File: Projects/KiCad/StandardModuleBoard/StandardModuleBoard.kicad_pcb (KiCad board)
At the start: 2 copper layers, 110 x 95 mm, 20 parts, among them J1 Conn_01x04_Pin, J2 Conn_01x04_Socket, J3 Micro_SD_Card_Det_Hirose_DM3AT, U1 NUCLEO-F303K8, U2 MCP2562-E-P, U3 24LC256

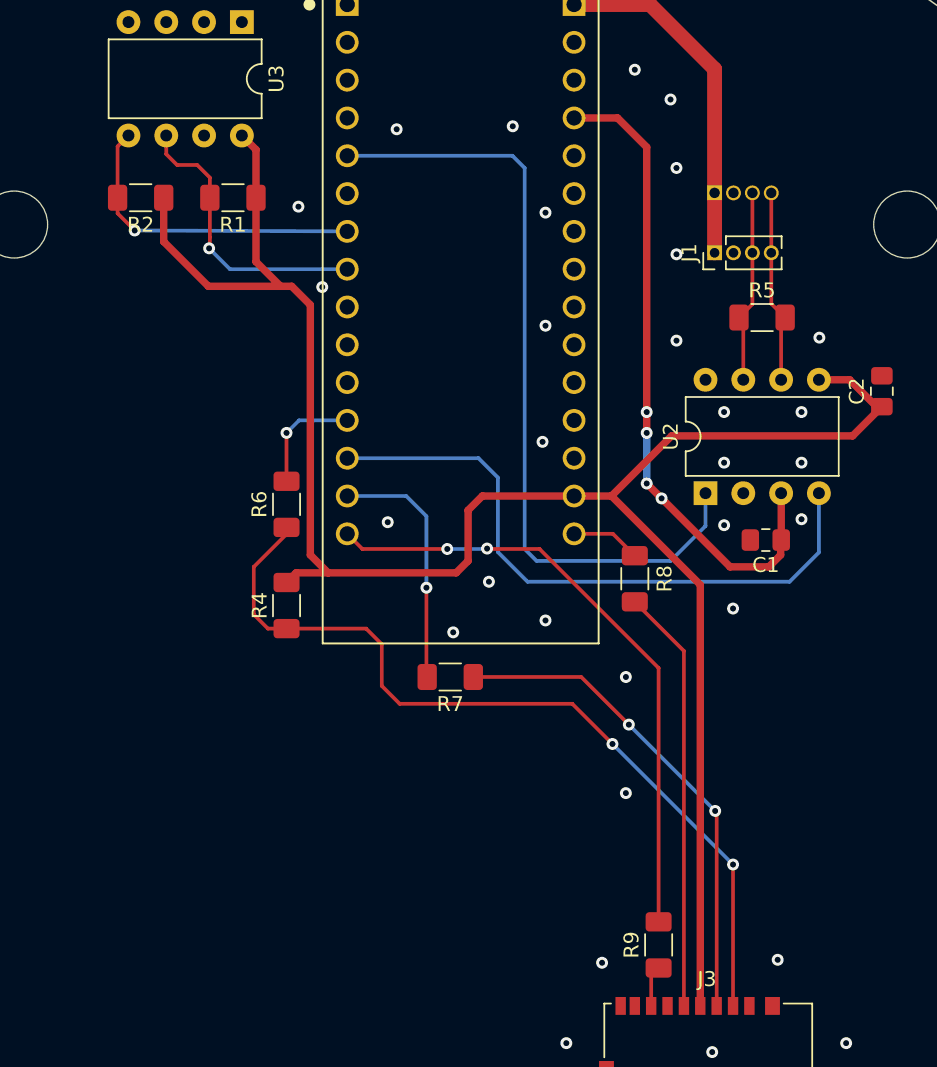
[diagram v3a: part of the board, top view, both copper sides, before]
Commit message: 標準モジュールにパイロットランプを追加
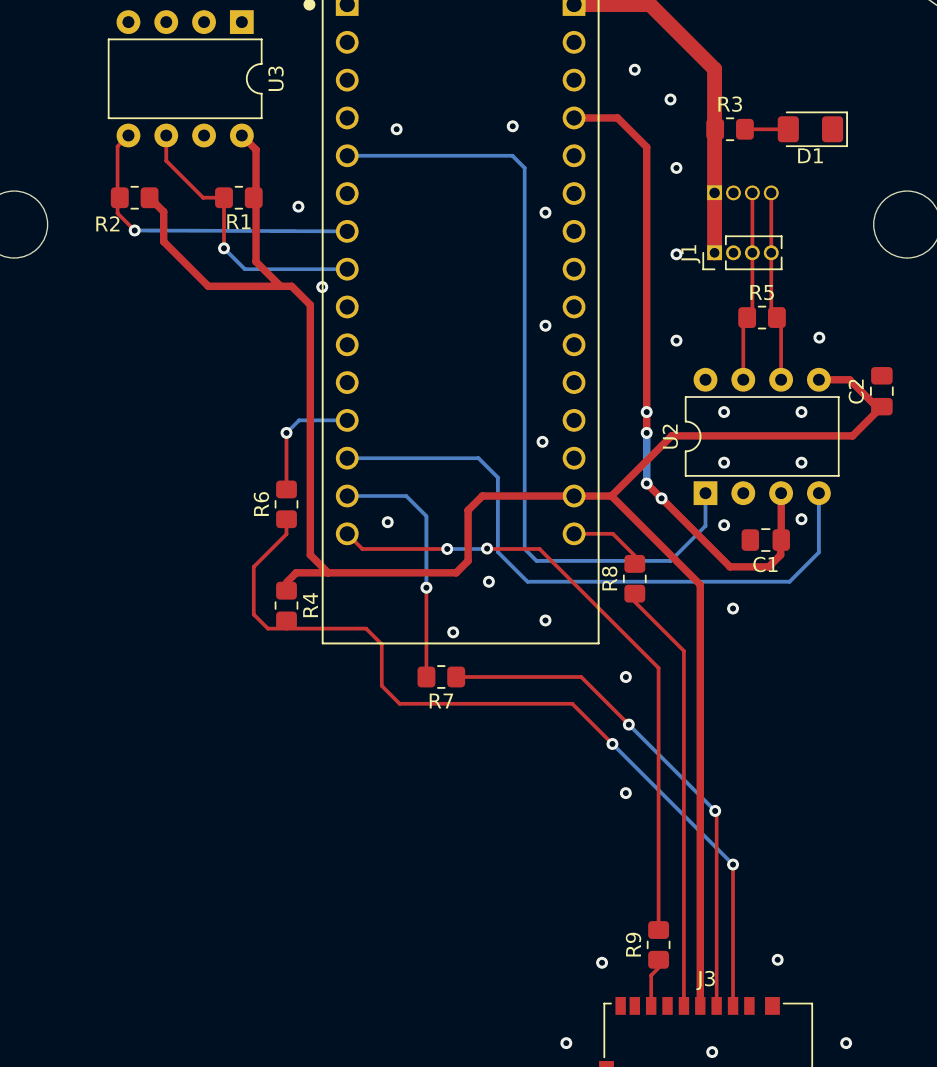
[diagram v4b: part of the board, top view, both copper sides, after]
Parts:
- added D1: LED, LED_SMD:LED_1206_3216Metric_Pad1.42x1.75mm_HandSolder, F.Cu at (172.0, 68.6)
- added R3: 2kΩ, Resistor_SMD:R_0805_2012Metric_Pad1.20x1.40mm_HandSolder, F.Cu at (166.6, 68.6)
- R1, R2, R4, R5, R6, R7, R8, R9: footprint Resistor_SMD:R_1206_3216Metric_Pad1.30x1.75mm_HandSolder -> Resistor_SMD:R_0805_2012Metric_Pad1.20x1.40mm_HandSolder
- moved R7 0.60 mm to (147.2, 105.4)
- moved R1 0.40 mm to (133.6, 73.2)
- moved R2 0.40 mm to (126.6, 73.2)
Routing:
- net Net-(D1-A): track 0.00 -> 2.91 mm
- net SPI_MOSI: track 33.1 -> 34.3 mm
